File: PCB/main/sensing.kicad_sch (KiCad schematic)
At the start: 0 parts

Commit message: Added sheet details to schematic
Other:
- company: (none) -> UCT
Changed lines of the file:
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@@
 (kicad_sch (version 20211123) (generator eeschema)
   (paper "A4")
+  (title_block
+    (date "2022-03-02")
+    (rev "v0.0")
+    (company "UCT")
+    (comment 2 "Group 7")
+    (comment 3 "@Checked By: ")
+    (comment 4 "@Authors: Ryan Jones, Alex Cargill & Devlin Trafford")
+  )
   (text "Sensors and supporting analog components, decoupling, pin assignments"
     (at 115.57 86.36 0)

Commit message: Sensing SubModule v0.01
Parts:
- added C4: C, symbol pspice:C
- added R17, R18: R, symbol Device:R
- added U3: DS18B20Z, Package_SO:SOIC-8_3.9x4.9mm_P1.27mm, symbol Sensor_Temperature:DS18B20Z
- added U4: ALS-PDIC15-21B/TR8, OptoDevice:Vishay_MINICAST-3Pin, symbol Sensor_Proximity:TSSP58038SS1XB
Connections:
- new net +3V3: R17.1, U3.3 (VDD), U4.3 (Vs)
- new net Analogue out: C4.1, R18.1, U4.1 (OUT)
- new net Digital out: R17.2, U3.4 (DQ)
- new net GND: C4.2, R18.2, U3.5 (GND), U4.2 (GND)
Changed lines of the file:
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@@
   (title_block
     (date "2022-03-04")
-    (rev "v0.0")
+    (rev "v0.01")
     (company "UCT")
     (comment 2 "Group 7")
@@
     (comment 4 "@Authors: Ryan Jones, Alex Cargill & Devlin Trafford")
   )
+  (junction (at 114.3 50.8) (diameter 0) (color 0 0 0 0)
+  )
+  (junction (at 121.92 38.1) (diameter 0) (color 0 0 0 0)
+  )
+  (junction (at 114.3 38.1) (diameter 0) (color 0 0 0 0)
+  )
+  (junction (at 121.92 50.8) (diameter 0) (color 0 0 0 0)
+  )
+  (junction (at 52.07 38.1) (diameter 0) (color 0 0 0 0)
+  )
+  (junction (at 41.91 30.48) (diameter 0) (color 0 0 0 0)
+  )
+  (polyline (pts (xy 80.01 11.43) (xy 80.01 54.61))
+    (stroke (width 0) (type default) (color 0 0 0 0))
+  )
+  (wire (pts (xy 109.22 43.18) (xy 110.49 43.18))
+    (stroke (width 0) (type default) (color 0 0 0 0))
+  )
+  (wire (pts (xy 114.3 50.8) (xy 114.3 45.72))
+    (stroke (width 0) (type default) (color 0 0 0 0))
+  )
+  (polyline (pts (xy 80.01 54.61) (xy 80.01 69.85))
+    (stroke (width 0) (type default) (color 0 0 0 0))
+  )
+  (wire (pts (xy 109.22 38.1) (xy 114.3 38.1))
+    (stroke (width 0) (type default) (color 0 0 0 0))
+  )
+  (wire (pts (xy 121.92 38.1) (xy 124.46 38.1))
+    (stroke (width 0) (type default) (color 0 0 0 0))
+  )
+  (polyline (pts (xy 80.01 69.85) (xy 152.4 69.85))
+    (stroke (width 0) (type default) (color 0 0 0 0))
+  )
+  (wire (pts (xy 49.53 38.1) (xy 52.07 38.1))
+    (stroke (width 0) (type default) (color 0 0 0 0))
+  )
+  (wire (pts (xy 41.91 27.94) (xy 41.91 30.48))
+    (stroke (width 0) (type default) (color 0 0 0 0))
+  )
+  (wire (pts (xy 114.3 50.8) (xy 121.92 50.8))
+    (stroke (width 0) (type default) (color 0 0 0 0))
+  )
+  (wire (pts (xy 110.49 43.18) (xy 110.49 50.8))
+    (stroke (width 0) (type default) (color 0 0 0 0))
+  )
+  (polyline (pts (xy 12.7 54.61) (xy 80.01 54.61))
+    (stroke (width 0) (type default) (color 0 0 0 0))
+  )
+  (wire (pts (xy 41.91 30.48) (xy 52.07 30.48))
+    (stroke (width 0) (type default) (color 0 0 0 0))
+  )
+  (wire (pts (xy 109.22 33.02) (xy 116.84 33.02))
+    (stroke (width 0) (type default) (color 0 0 0 0))
+  )
+  (wire (pts (xy 114.3 38.1) (xy 121.92 38.1))
+    (stroke (width 0) (type default) (color 0 0 0 0))
+  )
+  (polyline (pts (xy 152.4 11.43) (xy 152.4 69.85))
+    (stroke (width 0) (type default) (color 0 0 0 0))
+  )
+  (wire (pts (xy 110.49 50.8) (xy 114.3 50.8))
+    (stroke (width 0) (type default) (color 0 0 0 0))
+  )
+  (wire (pts (xy 52.07 38.1) (xy 63.5 38.1))
+    (stroke (width 0) (type default) (color 0 0 0 0))
+  )
   (text "Sensors and supporting analog components, decoupling, pin assignments"
     (at 115.57 86.36 0)
     (effects (font (size 1.27 1.27)) (justify left bottom))
   )
+  (label "ANALOGUE TEMPERATURE SENSOR ALS-PDIC15-21B-TR8" (at 90.17 15.24 0)
+    (effects (font (size 1.27 1.27)) (justify left bottom))
+  )
+  (label "Analogue out" (at 124.46 38.1 0)
+    (effects (font (size 1.27 1.27)) (justify left bottom))
+  )
+  (label "DIGITAL TEMPERATURE SENSOR DS18B20Z " (at 26.67 15.24 0)
+    (effects (font (size 1.27 1.27)) (justify left bottom))
+  )
+  (label "Digital out" (at 63.5 38.1 0)
+    (effects (font (size 1.27 1.27)) (justify left bottom))
+  )
+  (symbol (lib_id "power:+3.3V") (at 41.91 27.94 0) (unit 1)
+    (in_bom yes) (on_board yes) (fields_autoplaced)
+    (property "Reference" "#PWR0101" (id 0) (at 41.91 31.75 0)
+      (effects (font (size 1.27 1.27)) hide)
+    )
+    (property "Value" "+3.3V" (id 1) (at 41.91 22.86 0))
+    (property "Footprint" "" (id 2) (at 41.91 27.94 0)
+      (effects (font (size 1.27 1.27)) hide)
+    )
+    (property "Datasheet" "" (id 3) (at 41.91 27.94 0)
+      (effects (font (size 1.27 1.27)) hide)
+    )
+    (pin "1")
+  )
+  (symbol (lib_id "Sensor_Proximity:TSSP58038SS1XB") (at 99.06 38.1 0) (unit 1)
+    (in_bom yes) (on_board yes) (fields_autoplaced)
+    (property "Reference" "U4" (id 0) (at 97.325 26.67 0)
+      (effects (font (size 1.27 1.27)) hide)
+    )
+    (property "Value" "ALS-PDIC15-21B/TR8" (id 1) (at 97.325 29.21 0))
+    (property "Footprint" "OptoDevice:Vishay_MINICAST-3Pin" (id 2) (at 97.79 47.625 0)
+      (effects (font (size 1.27 1.27)) hide)
+    )
+    (property "Datasheet" "http://www.vishay.com/docs/82740/tssp58038ss1xb.pdf" (id 3) (at 115.57 30.48 0)
+      (effects (font (size 1.27 1.27)) hide)
+    )
+    (pin "1")
+    (pin "2")
+    (pin "3")
+  )
+  (symbol (lib_id "Device:R") (at 52.07 34.29 0) (unit 1)
+    (in_bom yes) (on_board yes) (fields_autoplaced)
+    (property "Reference" "R17" (id 0) (at 54.61 33.0199 0)
+      (effects (font (size 1.27 1.27)) (justify left) hide)
+    )
+    (property "Value" "R" (id 1) (at 54.61 34.2899 0)
+      (effects (font (size 1.27 1.27)) (justify left))
+    )
+    (property "Footprint" "" (id 2) (at 50.292 34.29 90)
+      (effects (font (size 1.27 1.27)) hide)
+    )
+    (property "Datasheet" "~" (id 3) (at 52.07 34.29 0)
+      (effects (font (size 1.27 1.27)) hide)
+    )
+    (pin "1")
+    (pin "2")
+  )
+  (symbol (lib_id "power:GND") (at 121.92 50.8 0) (unit 1)
+    (in_bom yes) (on_board yes) (fields_autoplaced)
+    (property "Reference" "#PWR0103" (id 0) (at 121.92 57.15 0)
+      (effects (font (size 1.27 1.27)) hide)
+    )
+    (property "Value" "GND" (id 1) (at 121.92 55.88 0))
+    (property "Footprint" "" (id 2) (at 121.92 50.8 0)
+      (effects (font (size 1.27 1.27)) hide)
+    )
+    (property "Datasheet" "" (id 3) (at 121.92 50.8 0)
+      (effects (font (size 1.27 1.27)) hide)
+    )
+    (pin "1")
+  )
+  (symbol (lib_id "pspice:C") (at 121.92 44.45 0) (unit 1)
+    (in_bom yes) (on_board yes) (fields_autoplaced)
+    (property "Reference" "C4" (id 0) (at 127 43.1799 0)
+      (effects (font (size 1.27 1.27)) (justify left) hide)
+    )
+    (property "Value" "C" (id 1) (at 127 44.4499 0)
+      (effects (font (size 1.27 1.27)) (justify left))
+    )
+    (property "Footprint" "" (id 2) (at 121.92 44.45 0)
+      (effects (font (size 1.27 1.27)) hide)
+    )
+    (property "Datasheet" "~" (id 3) (at 121.92 44.45 0)
+      (effects (font (size 1.27 1.27)) hide)
+    )
+    (pin "1")
+    (pin "2")
+  )
+  (symbol (lib_id "power:GND") (at 41.91 45.72 0) (unit 1)
+    (in_bom yes) (on_board yes) (fields_autoplaced)
+    (property "Reference" "#PWR0104" (id 0) (at 41.91 52.07 0)
+      (effects (font (size 1.27 1.27)) hide)
+    )
+    (property "Value" "GND" (id 1) (at 41.91 50.8 0))
+    (property "Footprint" "" (id 2) (at 41.91 45.72 0)
+      (effects (font (size 1.27 1.27)) hide)
+    )
+    (property "Datasheet" "" (id 3) (at 41.91 45.72 0)
+      (effects (font (size 1.27 1.27)) hide)
+    )
+    (pin "1")
+  )
+  (symbol (lib_id "Sensor_Temperature:DS18B20Z") (at 41.91 38.1 0) (unit 1)
+    (in_bom yes) (on_board yes) (fields_autoplaced)
+    (property "Reference" "U3" (id 0) (at 35.56 36.8299 0)
+      (effects (font (size 1.27 1.27)) (justify right) hide)
+    )
+    (property "Value" "DS18B20Z" (id 1) (at 35.56 38.0999 0)
+      (effects (font (size 1.27 1.27)) (justify right))
+    )
+    (property "Footprint" "Package_SO:SOIC-8_3.9x4.9mm_P1.27mm" (id 2) (at 16.51 44.45 0)
+      (effects (font (size 1.27 1.27)) hide)
+    )
+    (property "Datasheet" "http://datasheets.maximintegrated.com/en/ds/DS18B20.pdf" (id 3) (at 38.1 31.75 0)
+      (effects (font (size 1.27 1.27)) hide)
+    )
+    (pin "1")
+    (pin "2")
+    (pin "3")
+    (pin "4")
+    (pin "5")
+    (pin "6")
+    (pin "7")
+    (pin "8")
+  )
+  (symbol (lib_id "power:+3.3V") (at 116.84 33.02 0) (unit 1)
+    (in_bom yes) (on_board yes) (fields_autoplaced)
+    (property "Reference" "#PWR0102" (id 0) (at 116.84 36.83 0)
+      (effects (font (size 1.27 1.27)) hide)
+    )
+    (property "Value" "+3.3V" (id 1) (at 116.84 27.94 0))
+    (property "Footprint" "" (id 2) (at 116.84 33.02 0)
+      (effects (font (size 1.27 1.27)) hide)
+    )
+    (property "Datasheet" "" (id 3) (at 116.84 33.02 0)
+      (effects (font (size 1.27 1.27)) hide)
+    )
+    (pin "1")
+  )
+  (symbol (lib_id "Device:R") (at 114.3 41.91 0) (unit 1)
+    (in_bom yes) (on_board yes) (fields_autoplaced)
+    (property "Reference" "R18" (id 0) (at 116.84 40.6399 0)
+      (effects (font (size 1.27 1.27)) (justify left) hide)
+    )
+    (property "Value" "R" (id 1) (at 116.84 41.9099 0)
+      (effects (font (size 1.27 1.27)) (justify left))
+    )
+    (property "Footprint" "" (id 2) (at 112.522 41.91 90)
+      (effects (font (size 1.27 1.27)) hide)
+    )
+    (property "Datasheet" "~" (id 3) (at 114.3 41.91 0)
+      (effects (font (size 1.27 1.27)) hide)
+    )
+    (pin "1")
+    (pin "2")
+  )
 )

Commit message: Power v0.1, Sensing v0.1, uC Control v0.1, Simulations
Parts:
- renumbered C4 to C7, R17 to R14, R18 to R15, U3 to U2, U4 to U3
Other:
- note added: "ANALOGUE TEMPERATURE SENSOR ALS-PDIC15-21B-TR8"
- note added: "DIGITAL TEMPERATURE SENSOR DS18B20Z"
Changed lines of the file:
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@@
   (paper "A4")
   (title_block
-    (date "2022-03-04")
-    (rev "v0.01")
+    (date "2022-03-11")
+    (rev "v0.10")
     (company "UCT")
     (comment 2 "Group 7")
@@
     (stroke (width 0) (type default) (color 0 0 0 0))
   )
+  (text "ANALOGUE TEMPERATURE SENSOR ALS-PDIC15-21B-TR8" (at 81.28 15.24 0)
+    (effects (font (size 1.27 1.27)) (justify left bottom))
+  )
   (text "Sensors and supporting analog components, decoupling, pin assignments"
     (at 115.57 86.36 0)
     (effects (font (size 1.27 1.27)) (justify left bottom))
   )
-  (label "ANALOGUE TEMPERATURE SENSOR ALS-PDIC15-21B-TR8" (at 90.17 15.24 0)
+  (text "DIGITAL TEMPERATURE SENSOR DS18B20Z " (at 12.7 15.24 0)
     (effects (font (size 1.27 1.27)) (justify left bottom))
   )
@@
     (effects (font (size 1.27 1.27)) (justify left bottom))
   )
-  (label "DIGITAL TEMPERATURE SENSOR DS18B20Z " (at 26.67 15.24 0)
-    (effects (font (size 1.27 1.27)) (justify left bottom))
-  )
   (label "Digital out" (at 63.5 38.1 0)
     (effects (font (size 1.27 1.27)) (justify left bottom))
@@
   (symbol (lib_id "power:+3.3V") (at 41.91 27.94 0) (unit 1)
     (in_bom yes) (on_board yes) (fields_autoplaced)
-    (property "Reference" "#PWR0101" (id 0) (at 41.91 31.75 0)
+    (property "Reference" "#PWR034" (id 0) (at 41.91 31.75 0)
       (effects (font (size 1.27 1.27)) hide)
     )
@@
   (symbol (lib_id "Sensor_Proximity:TSSP58038SS1XB") (at 99.06 38.1 0) (unit 1)
     (in_bom yes) (on_board yes) (fields_autoplaced)
-    (property "Reference" "U4" (id 0) (at 97.325 26.67 0)
+    (property "Reference" "U3" (id 0) (at 97.325 26.67 0)
       (effects (font (size 1.27 1.27)) hide)
     )
@@
   (symbol (lib_id "Device:R") (at 52.07 34.29 0) (unit 1)
     (in_bom yes) (on_board yes) (fields_autoplaced)
-    (property "Reference" "R17" (id 0) (at 54.61 33.0199 0)
+    (property "Reference" "R14" (id 0) (at 54.61 33.0199 0)
       (effects (font (size 1.27 1.27)) (justify left) hide)
     )
@@
   (symbol (lib_id "power:GND") (at 121.92 50.8 0) (unit 1)
     (in_bom yes) (on_board yes) (fields_autoplaced)
-    (property "Reference" "#PWR0103" (id 0) (at 121.92 57.15 0)
+    (property "Reference" "#PWR037" (id 0) (at 121.92 57.15 0)
       (effects (font (size 1.27 1.27)) hide)
     )
@@
   (symbol (lib_id "pspice:C") (at 121.92 44.45 0) (unit 1)
     (in_bom yes) (on_board yes) (fields_autoplaced)
-    (property "Reference" "C4" (id 0) (at 127 43.1799 0)
+    (property "Reference" "C7" (id 0) (at 127 43.1799 0)
       (effects (font (size 1.27 1.27)) (justify left) hide)
     )
@@
   (symbol (lib_id "power:GND") (at 41.91 45.72 0) (unit 1)
     (in_bom yes) (on_board yes) (fields_autoplaced)
-    (property "Reference" "#PWR0104" (id 0) (at 41.91 52.07 0)
+    (property "Reference" "#PWR036" (id 0) (at 41.91 52.07 0)
       (effects (font (size 1.27 1.27)) hide)
     )
@@
   (symbol (lib_id "Sensor_Temperature:DS18B20Z") (at 41.91 38.1 0) (unit 1)
     (in_bom yes) (on_board yes) (fields_autoplaced)
-    (property "Reference" "U3" (id 0) (at 35.56 36.8299 0)
+    (property "Reference" "U2" (id 0) (at 35.56 36.8299 0)
       (effects (font (size 1.27 1.27)) (justify right) hide)
     )
@@
   (symbol (lib_id "power:+3.3V") (at 116.84 33.02 0) (unit 1)
     (in_bom yes) (on_board yes) (fields_autoplaced)
-    (property "Reference" "#PWR0102" (id 0) (at 116.84 36.83 0)
+    (property "Reference" "#PWR035" (id 0) (at 116.84 36.83 0)
       (effects (font (size 1.27 1.27)) hide)
     )
@@
   (symbol (lib_id "Device:R") (at 114.3 41.91 0) (unit 1)
     (in_bom yes) (on_board yes) (fields_autoplaced)
-    (property "Reference" "R18" (id 0) (at 116.84 40.6399 0)
+    (property "Reference" "R15" (id 0) (at 116.84 40.6399 0)
       (effects (font (size 1.27 1.27)) (justify left) hide)
     )

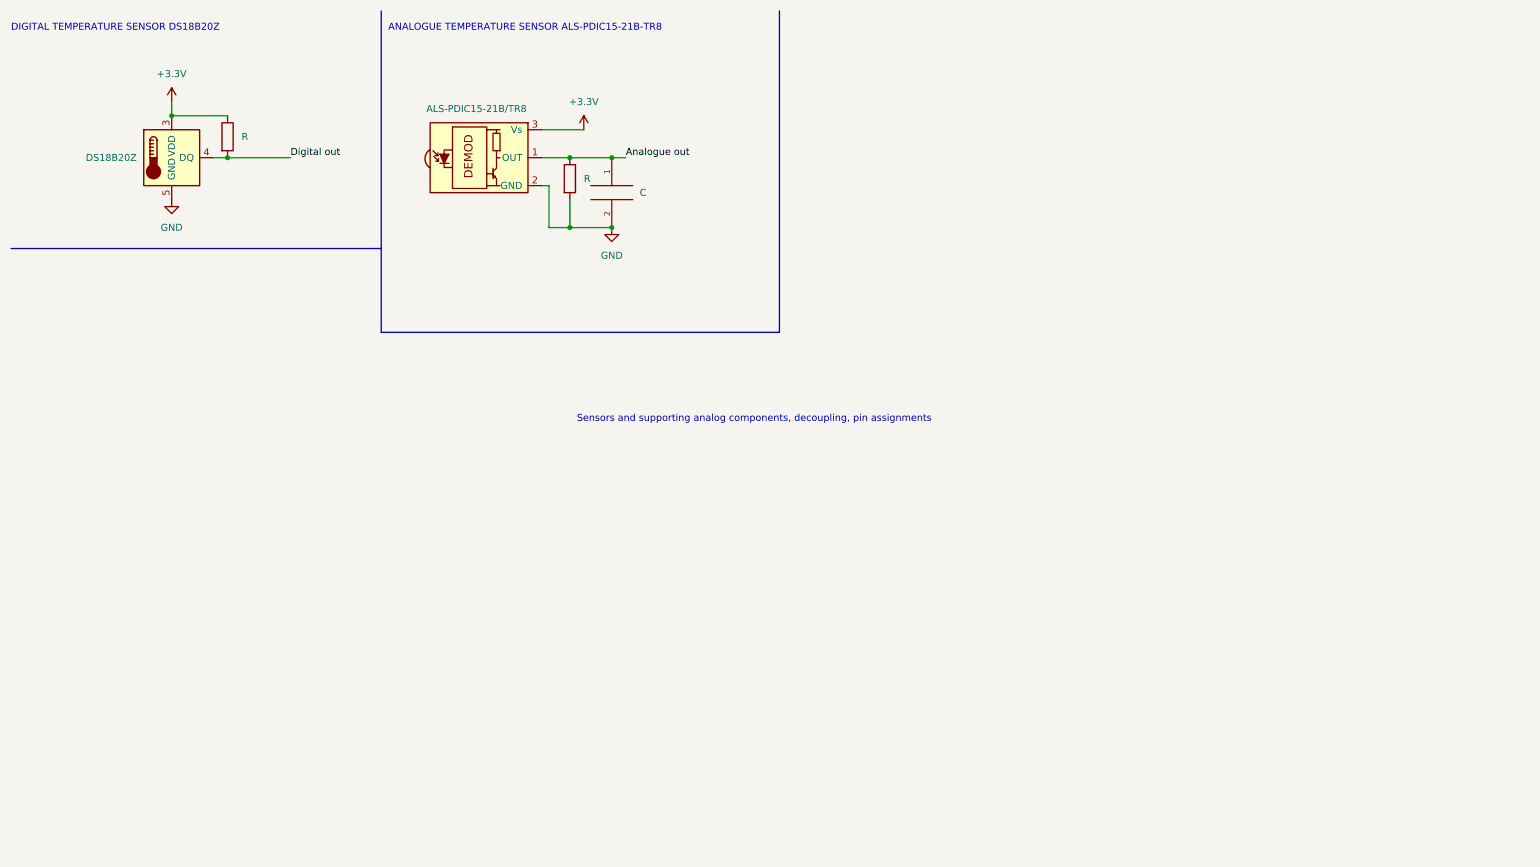
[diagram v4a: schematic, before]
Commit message: Power v0.1, Sensing v0.1, uC Control v0.1, ERC
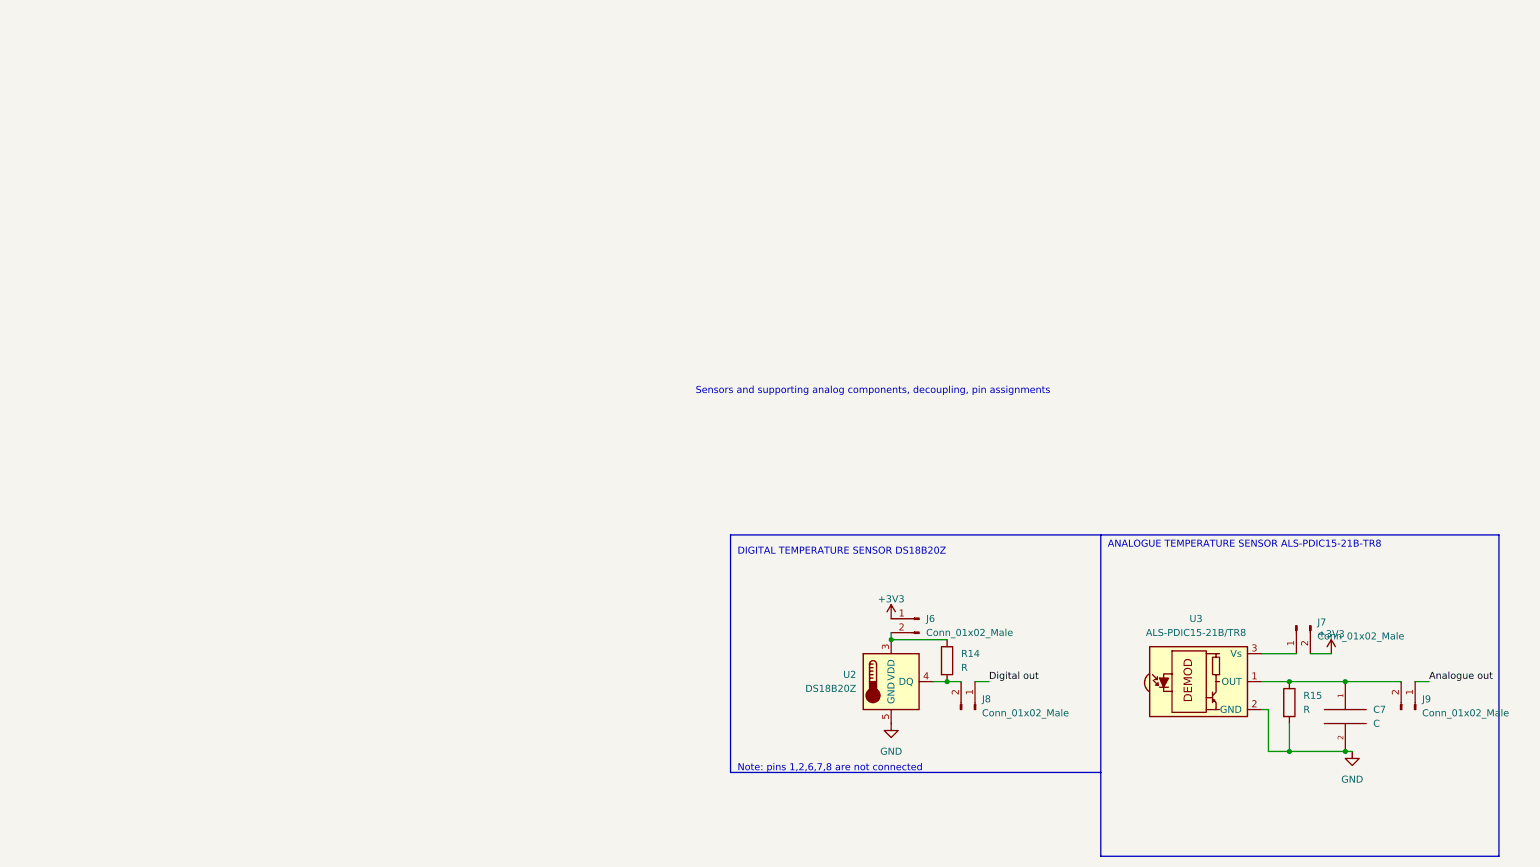
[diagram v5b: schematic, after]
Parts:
- added J6, J7, J8, J9: Conn_01x02_Male, symbol Connector:Conn_01x02_Male
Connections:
- net +3V3: now also J6.1 (Pin_1), J7.2 (Pin_2); no longer R14.1, U2.3 (VDD), U3.3 (Vs)
- net Analogue out: now also J9.1 (Pin_1); no longer C7.1, R15.1, U3.1 (OUT)
- net Digital out: now also J8.1 (Pin_1); no longer R14.2, U2.4 (DQ)
- new net: C7.1, J9.2 (Pin_2), R15.1, U3.1 (OUT)
- new net: J7.1 (Pin_1), U3.3 (Vs)
- new net: J6.2 (Pin_2), R14.1, U2.3 (VDD)
- new net: J8.2 (Pin_2), R14.2, U2.4 (DQ)
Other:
- note added: "Note: pins 1,2,6,7,8 are not connected"
